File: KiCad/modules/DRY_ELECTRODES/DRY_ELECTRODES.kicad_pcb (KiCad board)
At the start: 4 copper layers, 19 x 11.5 mm, 8 parts, among them J1 Conn_01x01_Pin, J2 Conn_01x01_Pin, J3 Conn_01x01_Pin, J4 Conn_01x01_Pin, J5 Conn_01x01_Pin, J6 Conn_01x01_Pin, J7 Conn_01x01_Pin, J8 Conn_01x01_Pin

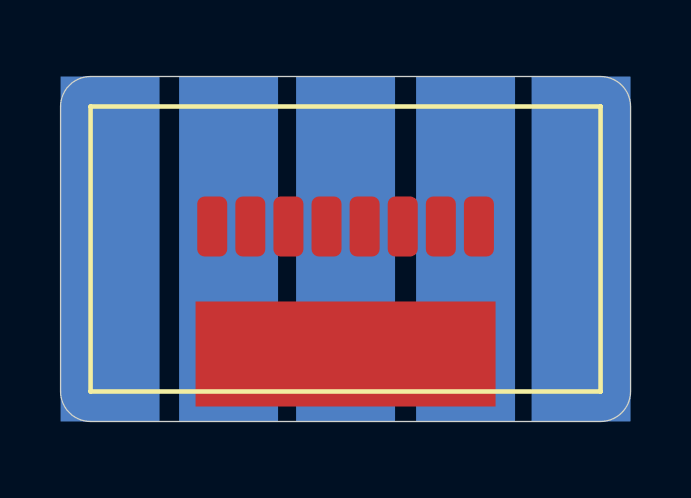
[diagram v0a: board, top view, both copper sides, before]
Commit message: some cleaning + edge plating dry electrode
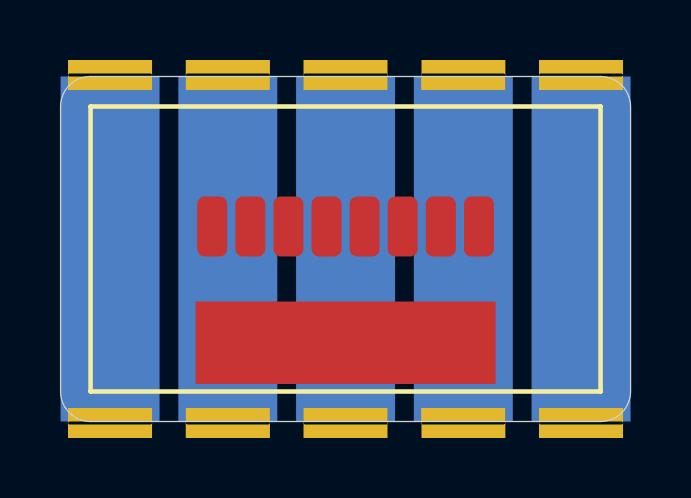
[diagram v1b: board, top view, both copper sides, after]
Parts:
- added ?: , , F.Cu at (96.1, 95.0)
- added ?: , , F.Cu at (92.2, 95.0)
- added ?: , , F.Cu at (107.8, 95.0)
- added ?: , , F.Cu at (103.9, 95.0)
- added ?: , , F.Cu at (100.0, 95.0)
- added REF**: PinHeader_1x01_P2.54mm_Vertical, Connector_PinHeader_2.54mm:PinHeader_1x01_P2.54mm_Vertical, F.Cu at (100.0, 106.5)
- added REF**: PinHeader_1x01_P2.54mm_Vertical, Connector_PinHeader_2.54mm:PinHeader_1x01_P2.54mm_Vertical, F.Cu at (104.4, 106.5)
- added REF**: PinHeader_1x01_P2.54mm_Vertical, Connector_PinHeader_2.54mm:PinHeader_1x01_P2.54mm_Vertical, F.Cu at (96.6, 106.5)
- added REF**: PinHeader_1x01_P2.54mm_Vertical, Connector_PinHeader_2.54mm:PinHeader_1x01_P2.54mm_Vertical, F.Cu at (92.2, 106.5)
- added REF**: PinHeader_1x01_P2.54mm_Vertical, Connector_PinHeader_2.54mm:PinHeader_1x01_P2.54mm_Vertical, F.Cu at (107.8, 106.5)

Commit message: lot of updates on ads93,flex,commod,pad
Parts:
- removed ? (x5): , 
- removed REF** (x5): PinHeader_1x01_P2.54mm_Vertical, Connector_PinHeader_2.54mm:PinHeader_1x01_P2.54mm_Vertical
- added I1: smd_insert, 00_Custom:insert_1.2mm, F.Cu at (22.5, 30.5)
- added I2: smd_insert, 00_Custom:insert_1.2mm, F.Cu at (37.5, 30.5)
- added I3: smd_insert, 00_Custom:insert_1.2mm, F.Cu at (22.5, 37.5)
- added I4: smd_insert, 00_Custom:insert_1.2mm, F.Cu at (37.5, 37.5)
- added kibuzzard-658AACB7: G***, kibuzzard-658AACB7, F.Cu at (30.0, 37.3)
- moved J1 96.0 mm to (25.5, 34.3)
- moved J2 96.0 mm to (26.8, 34.3)
- moved J3 96.0 mm to (28.1, 34.3)
- moved J4 96.0 mm to (29.3, 34.3)
- moved J5 96.0 mm to (30.6, 34.3)
- moved J6 96.0 mm to (31.9, 34.3)
- moved J7 96.0 mm to (33.1, 34.3)
- moved J8 96.0 mm to (34.4, 34.3)
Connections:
- J1 pad 1: unconnected-(J1-Pin_1-Pad1) -> /in1
- J2 pad 1: unconnected-(J2-Pin_1-Pad1) -> /in2
- J3 pad 1: unconnected-(J3-Pin_1-Pad1) -> /in3
- J4 pad 1: unconnected-(J4-Pin_1-Pad1) -> /in4
- J5 pad 1: unconnected-(J5-Pin_1-Pad1) -> /in5
- J6 pad 1: unconnected-(J6-Pin_1-Pad1) -> /in6
- J7 pad 1: unconnected-(J7-Pin_1-Pad1) -> /in7
- J8 pad 1: unconnected-(J8-Pin_1-Pad1) -> /in8
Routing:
- net /in7: track 0.00 -> 4.56 mm, vias 0 -> 3
- net /in2: track 0.00 -> 4.20 mm, vias 0 -> 3
- net /in8: track 0.00 -> 3.37 mm, vias 0 -> 3
- net /in1: track 0.00 -> 2.85 mm, vias 0 -> 3
- net /in5: track 0.00 -> 2.37 mm, vias 0 -> 3
- net /in6: track 0.00 -> 1.57 mm, vias 0 -> 3
- net /in4: track 0.00 -> 1.52 mm, vias 0 -> 3
- net /in3: track 0.00 -> 1.52 mm, vias 0 -> 3
- net GND: vias 0 -> 4
- added copper zone on B.Cu, net /in1
- added copper zone on F.Cu, net /in1
- added copper zone on B.Cu, net /in2
- added copper zone on F.Cu, net /in2
- added copper zone on B.Cu, net /in3
- added copper zone on F.Cu, net /in3
- added copper zone on B.Cu, net /in4
- added copper zone on F.Cu, net /in4
- added copper zone on B.Cu, net /in5
- added copper zone on F.Cu, net /in5
- added copper zone on B.Cu, net /in6
- added copper zone on F.Cu, net /in6
- added copper zone on B.Cu, net /in7
- added copper zone on F.Cu, net /in7
- added copper zone on B.Cu, net /in8
- added copper zone on F.Cu, net /in8
- added copper zone on F.Cu, net GND
- added copper zone on In1.Cu, net GND
- added copper zone on In2.Cu, net GND
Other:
- board size 19 x 11.5 mm -> 20 x 12 mm
- board text added: "1"
- board text added: "2"
- board text added: "3"
- board text added: "4"
- board text added: "5"
- board text added: "6"
- board text added: "7"
- board text added: "8"

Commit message: INA331 IMUICM
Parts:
- added J10: Conn_01x01_Pin, 00_custom-footprints:SolderWirePad_1x01_SMD_1x2mm, F.Cu at (26.2, 34.2)
- added J11: Conn_01x01_Pin, 00_custom-footprints:SolderWirePad_1x01_SMD_1x2mm, F.Cu at (27.8, 34.2)
- added J12: Conn_01x01_Pin, 00_custom-footprints:SolderWirePad_1x01_SMD_1x2mm, F.Cu at (29.2, 34.2)
- added J13: Conn_01x01_Pin, 00_custom-footprints:SolderWirePad_1x01_SMD_1x2mm, F.Cu at (30.8, 34.2)
- added J14: Conn_01x01_Pin, 00_custom-footprints:SolderWirePad_1x01_SMD_1x2mm, F.Cu at (32.2, 34.2)
- added J15: Conn_01x01_Pin, 00_custom-footprints:SolderWirePad_1x01_SMD_1x2mm, F.Cu at (33.8, 34.2)
- added J16: Conn_01x01_Pin, 00_custom-footprints:SolderWirePad_1x01_SMD_1x2mm, F.Cu at (35.2, 34.2)
- added J9: Conn_01x01_Pin, 00_custom-footprints:SolderWirePad_1x01_SMD_1x2mm, F.Cu at (24.8, 34.2)
- I1, I2, I3, I4: footprint 00_Custom:insert_1.2mm -> 00_custom-footprints:insert_1.2mm
- J1, J2, J3, J4, J5, J6, J7, J8: footprint Connector_Wire:SolderWirePad_1x01_SMD_1x2mm -> 00_custom-footprints:SolderWirePad_1x01_SMD_1x2mm
- moved J8 1.00 mm to (35.2, 33.8)
- moved J1 0.93 mm to (24.8, 33.8)
- moved J7 0.82 mm to (33.8, 33.8)
- moved J2 0.77 mm to (26.2, 33.8)
- moved J6 0.67 mm to (32.2, 33.8)
- moved J3 0.63 mm to (27.8, 33.8)
- moved J5 0.57 mm to (30.8, 33.8)
- moved J4 0.56 mm to (29.2, 33.8)
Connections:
- net /in1 renamed /in1-
- net /in2 renamed /in2-
- net /in3 renamed /in3-
- net /in4 renamed /in4-
- net /in5 renamed /in5-
- net /in6 renamed /in6-
- net /in7 renamed /in7-
- net /in8 renamed /in8-
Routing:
- net /in2-: track 4.20 -> 0.00 mm, vias 3 -> 2
- net /in2+: track 0.00 -> 4.20 mm, vias 0 -> 1
- net /in8-: track 3.37 -> 0.00 mm, vias 3 -> 2
- net /in8+: track 0.00 -> 3.37 mm, vias 0 -> 1
- net /in6-: track 1.57 -> 0.00 mm, vias 3 -> 2
- net /in6+: track 0.00 -> 1.57 mm, vias 0 -> 1
- net /in4-: track 1.52 -> 0.00 mm, vias 3 -> 2
- net /in4+: track 0.00 -> 1.52 mm, vias 0 -> 1
- net /in3-: track 1.52 -> 0.00 mm, vias 3 -> 2
- net /in3+: track 0.00 -> 1.52 mm, vias 0 -> 1

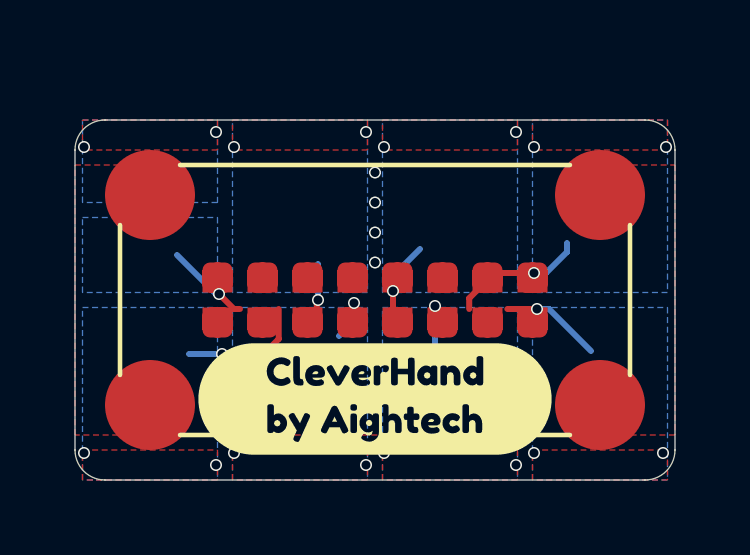
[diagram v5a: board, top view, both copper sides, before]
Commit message: jack, dry electrode
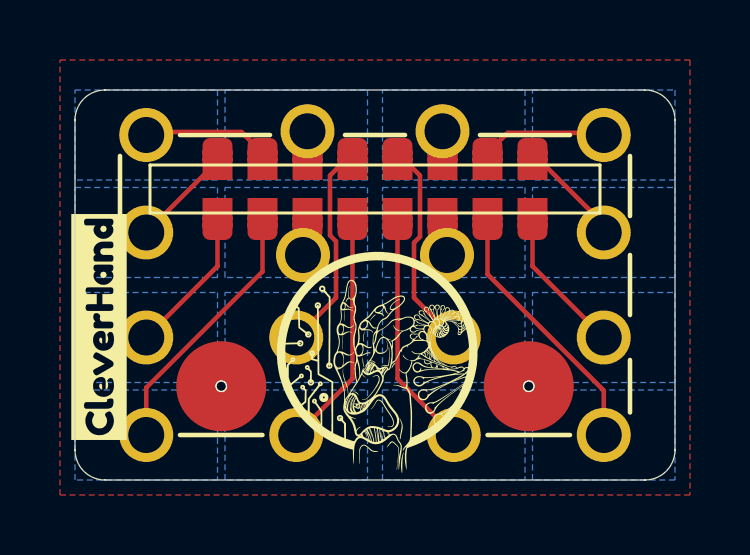
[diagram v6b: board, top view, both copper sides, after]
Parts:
- removed I1, I2: smd_insert, 00_custom-footprints:insert_1.2mm
- removed kibuzzard-658AACB7: G***, kibuzzard-658AACB7
- added J17: Conn_01x01_Pin, 00_custom-footprints:Pin_D1.2mm_pogo, F.Cu at (22.4, 31.8)
- added J18: Conn_01x01_Pin, 00_custom-footprints:Pin_D1.2mm_pogo, F.Cu at (22.4, 28.5)
- added J19: Conn_01x01_Pin, 00_custom-footprints:Pin_D1.2mm_pogo, F.Cu at (27.8, 28.4)
- added J20: Conn_01x01_Pin, 00_custom-footprints:Pin_D1.2mm_pogo, F.Cu at (27.4, 35.2)
- added J21: Conn_01x01_Pin, 00_custom-footprints:Pin_D1.2mm_pogo, F.Cu at (32.6, 35.2)
- added J22: Conn_01x01_Pin, 00_custom-footprints:Pin_D1.2mm_pogo, F.Cu at (32.2, 28.4)
- added J23: Conn_01x01_Pin, 00_custom-footprints:Pin_D1.2mm_pogo, F.Cu at (37.6, 28.5)
- added J24: Conn_01x01_Pin, 00_custom-footprints:Pin_D1.2mm_pogo, F.Cu at (37.6, 31.8)
- added J25: Conn_01x01_Pin, 00_custom-footprints:Pin_D1.2mm_pogo, F.Cu at (22.4, 35.2)
- added J26: Conn_01x01_Pin, 00_custom-footprints:Pin_D1.2mm_pogo, F.Cu at (22.4, 38.5)
- added J27: Conn_01x01_Pin, 00_custom-footprints:Pin_D1.2mm_pogo, F.Cu at (27.6, 32.5)
- added J28: Conn_01x01_Pin, 00_custom-footprints:Pin_D1.2mm_pogo, F.Cu at (27.4, 38.5)
- added J29: Conn_01x01_Pin, 00_custom-footprints:Pin_D1.2mm_pogo, F.Cu at (32.6, 38.5)
- added J30: Conn_01x01_Pin, 00_custom-footprints:Pin_D1.2mm_pogo, F.Cu at (32.4, 32.5)
- added J31: Conn_01x01_Pin, 00_custom-footprints:Pin_D1.2mm_pogo, F.Cu at (37.6, 38.5)
- added J32: Conn_01x01_Pin, 00_custom-footprints:Pin_D1.2mm_pogo, F.Cu at (37.6, 35.2)
- added REF**: logo_aightech, 00_custom-footprints:logo_aightech, F.Cu at (30.1, 35.9)
- added kibuzzard-660706DE: G***, kibuzzard-660706DE, F.Cu at (20.8, 34.9)
- moved J1 4.15 mm to (24.8, 29.6)
- moved J2 4.15 mm to (26.2, 29.6)
- moved J3 4.15 mm to (27.8, 29.6)
- moved J4 4.15 mm to (29.2, 29.6)
- moved J5 4.15 mm to (30.8, 29.6)
- moved J6 4.15 mm to (32.2, 29.6)
- moved J7 4.15 mm to (33.8, 29.6)
- moved J8 4.15 mm to (35.2, 29.6)
- moved J10 3.25 mm to (26.2, 31.0)
- moved J11 3.25 mm to (27.8, 31.0)
- moved J12 3.25 mm to (29.2, 31.0)
- moved J13 3.25 mm to (30.8, 31.0)
- moved J14 3.25 mm to (32.2, 31.0)
- moved J15 3.25 mm to (33.8, 31.0)
- moved J16 3.25 mm to (35.2, 31.0)
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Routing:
- net /in7+: track 0.00 -> 8.61 mm
- net /in5+: track 0.00 -> 7.78 mm
- net /in4-: track 0.00 -> 7.09 mm, vias 2 -> 0
- net /in4+: track 1.52 -> 7.78 mm, vias 1 -> 0
- net /in1+: track 0.00 -> 4.73 mm
- net /in5-: track 2.37 -> 7.09 mm, vias 3 -> 0
- net /in2+: track 4.20 -> 8.61 mm, vias 1 -> 0
- net /in2-: track 0.00 -> 4.21 mm, vias 2 -> 0
- net /in8-: track 0.00 -> 3.63 mm, vias 2 -> 0
- net /in6+: track 1.57 -> 0.00 mm, vias 1 -> 0
- net /in3+: track 1.52 -> 0.00 mm, vias 1 -> 0
- net /in8+: track 3.37 -> 4.73 mm, vias 1 -> 0
- net /in1-: track 2.85 -> 3.63 mm, vias 3 -> 0
- net /in7-: track 4.56 -> 4.18 mm, vias 3 -> 0
- net GND: vias 4 -> 2
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- added copper zone on B.Cu, net /in1+
- added copper zone on B.Cu, net /in2+
- added copper zone on B.Cu, net /in3+
- added copper zone on B.Cu, net /in4+
- added copper zone on B.Cu, net /in5+
- added copper zone on B.Cu, net /in6+
- added copper zone on B.Cu, net /in7+
- added copper zone on B.Cu, net /in8+
- removed copper zone on F.Cu, net /in1-
- removed copper zone on F.Cu, net /in2-
- removed copper zone on F.Cu, net /in3-
- removed copper zone on F.Cu, net /in4-
- removed copper zone on F.Cu, net /in5-
- removed copper zone on F.Cu, net /in6-
- removed copper zone on F.Cu, net /in7-
- removed copper zone on F.Cu, net /in8-
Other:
- board size 20 x 12 mm -> 20 x 13 mm
- board text added: "1+"
- board text added: "1-"
- board text added: "2+"
- board text added: "2-"
- board text added: "3+"
- board text added: "3-"
- board text added: "4+"
- board text added: "4-"
- board text added: "5+"
- board text added: "5-"
- board text added: "6+"
- board text added: "6-"
- board text added: "7+"
- board text added: "7-"
- board text added: "8+"
- board text added: "8-"
- board text removed: "1"
- board text removed: "2"
- board text removed: "3"
- board text removed: "4"
- board text removed: "5"
- board text removed: "6"
- board text removed: "7"
- board text removed: "8"

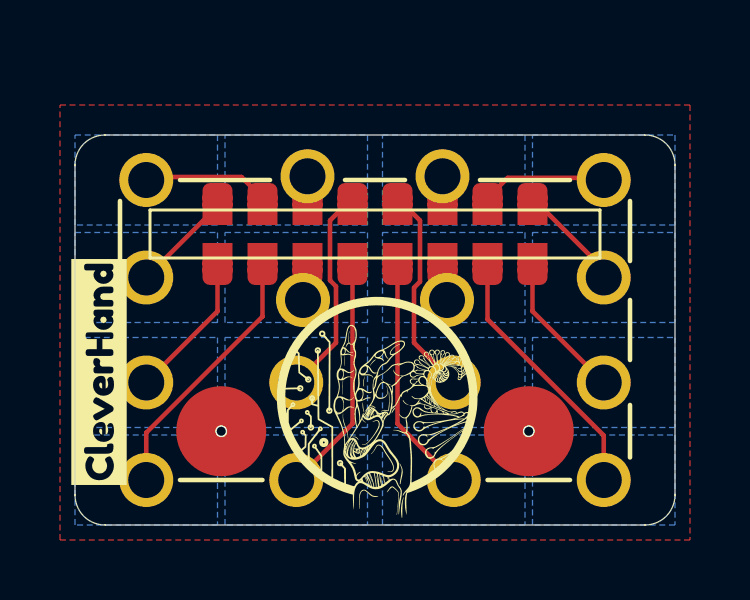
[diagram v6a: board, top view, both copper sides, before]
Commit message: refactor and fixing most of the modules
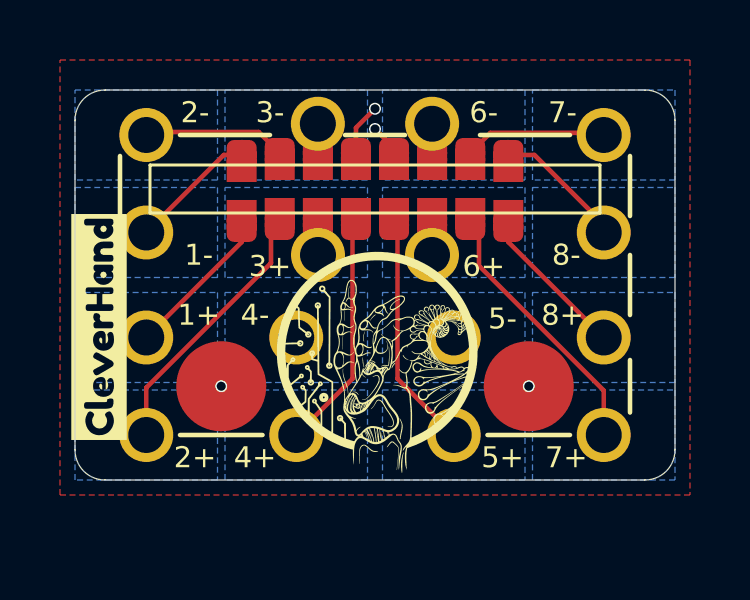
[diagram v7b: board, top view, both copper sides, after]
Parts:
- moved J19 1.78 mm to (28.1, 26.6)
- moved J22 1.78 mm to (31.9, 26.6)
- moved J1 1.65 mm to (25.6, 28.2)
- moved J8 1.65 mm to (34.4, 28.2)
- moved J16 1.65 mm to (34.4, 29.6)
- moved J9 1.65 mm to (25.6, 29.6)
- moved J15 1.61 mm to (33.2, 29.5)
- moved J7 1.61 mm to (33.2, 28.1)
- moved J10 1.61 mm to (26.8, 29.5)
- moved J2 1.61 mm to (26.8, 28.1)
- moved J27 1.58 mm to (28.1, 31.0)
- moved J30 1.58 mm to (31.9, 31.0)
- moved J11 1.54 mm to (28.1, 29.5)
- moved J14 1.54 mm to (31.9, 29.5)
- moved J3 1.54 mm to (28.1, 28.1)
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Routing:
- net /in4-: track 7.09 -> 10.5 mm, vias 0 -> 1
- net /in5-: track 7.09 -> 9.10 mm, vias 0 -> 1
- net /in8-: track 3.63 -> 4.41 mm
- net /in1-: track 3.63 -> 4.25 mm
- net /in7-: track 4.18 -> 4.76 mm
- net /in2-: track 4.21 -> 4.78 mm
